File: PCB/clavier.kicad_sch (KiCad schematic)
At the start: 0 parts

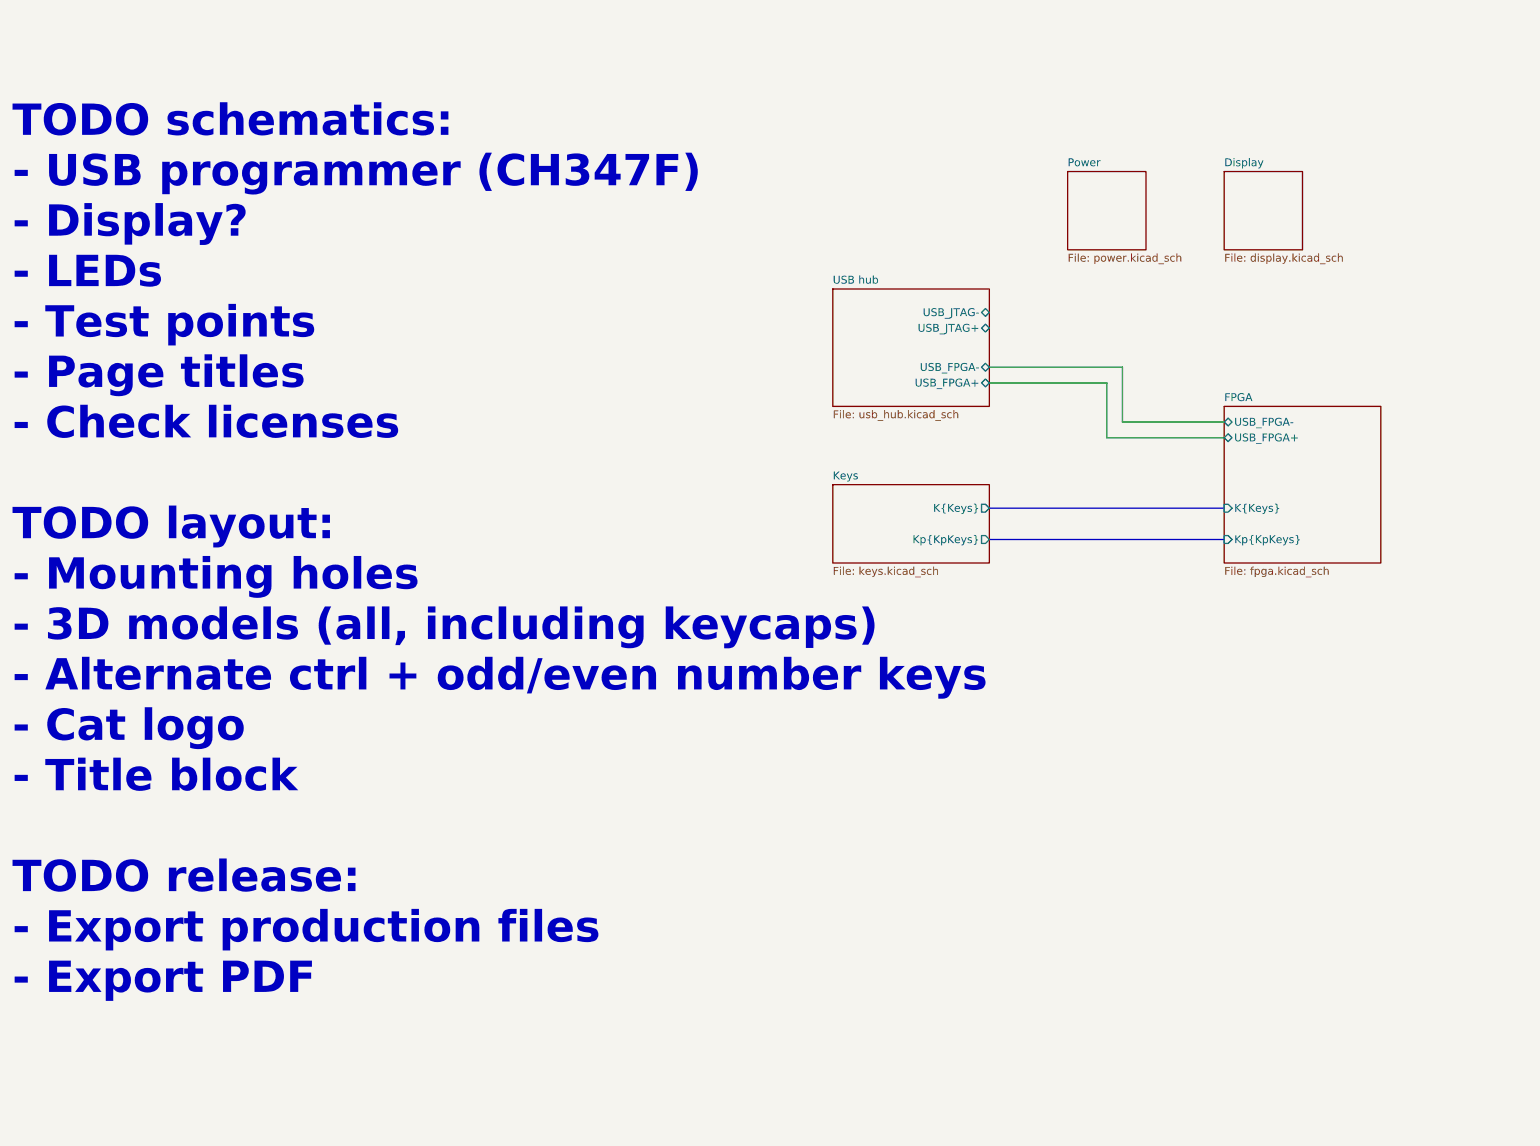
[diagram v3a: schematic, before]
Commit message: Add the USB to JTAG bridge
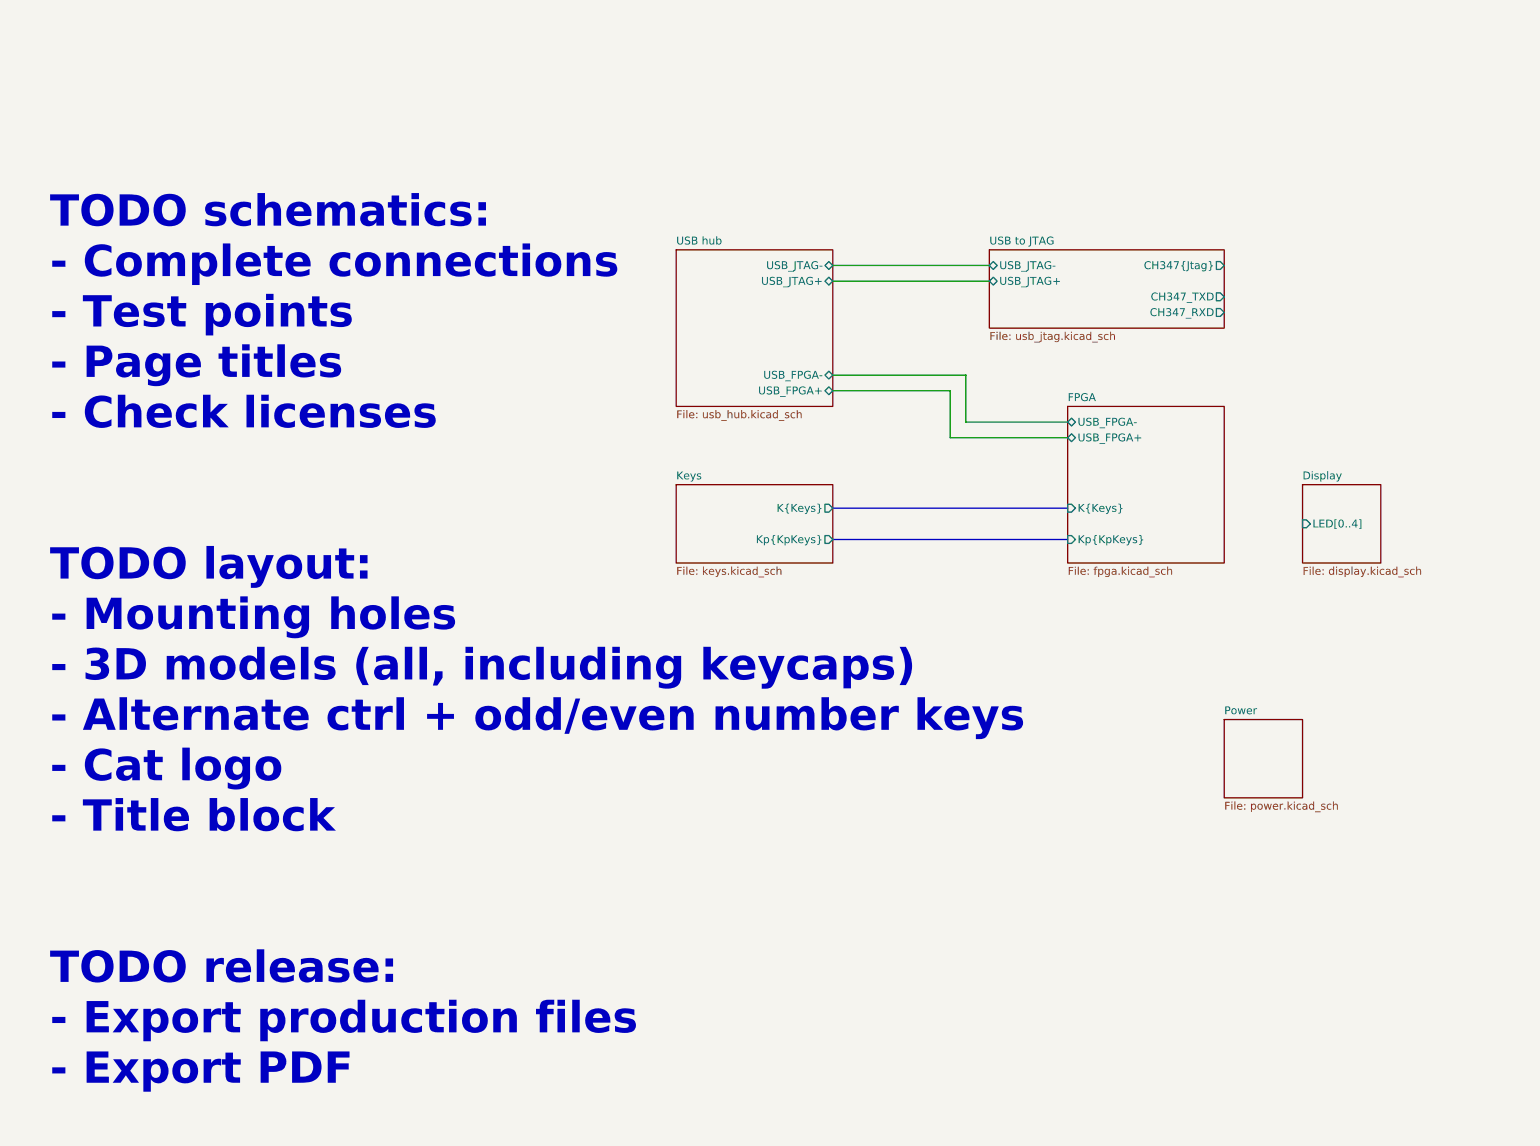
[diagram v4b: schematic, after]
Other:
- added sheet USB to JTAG (usb_jtag.kicad_sch)
- sheet Display ports: added LED[0..4]; removed none
- note added: "TODO schematics: - Complete connections - Test points - Page titles - Check licenses TODO layout: - Mounting holes - 3D models (all, including keycaps) - Alternate ctrl + odd/even number keys - Cat logo - Title block TODO release: - Export production files - Export PDF"
- note removed: "TODO schematics: - USB programmer (CH347F) - Display? - LEDs - Test points - Page titles - Check licenses TODO layout: - Mounting holes - 3D models (all, including keycaps) - Alternate ctrl + odd/even number keys - Cat logo - Title block TODO release: - Export production files - Export PDF"

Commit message: Improve the CH347F schematics and added 3D models
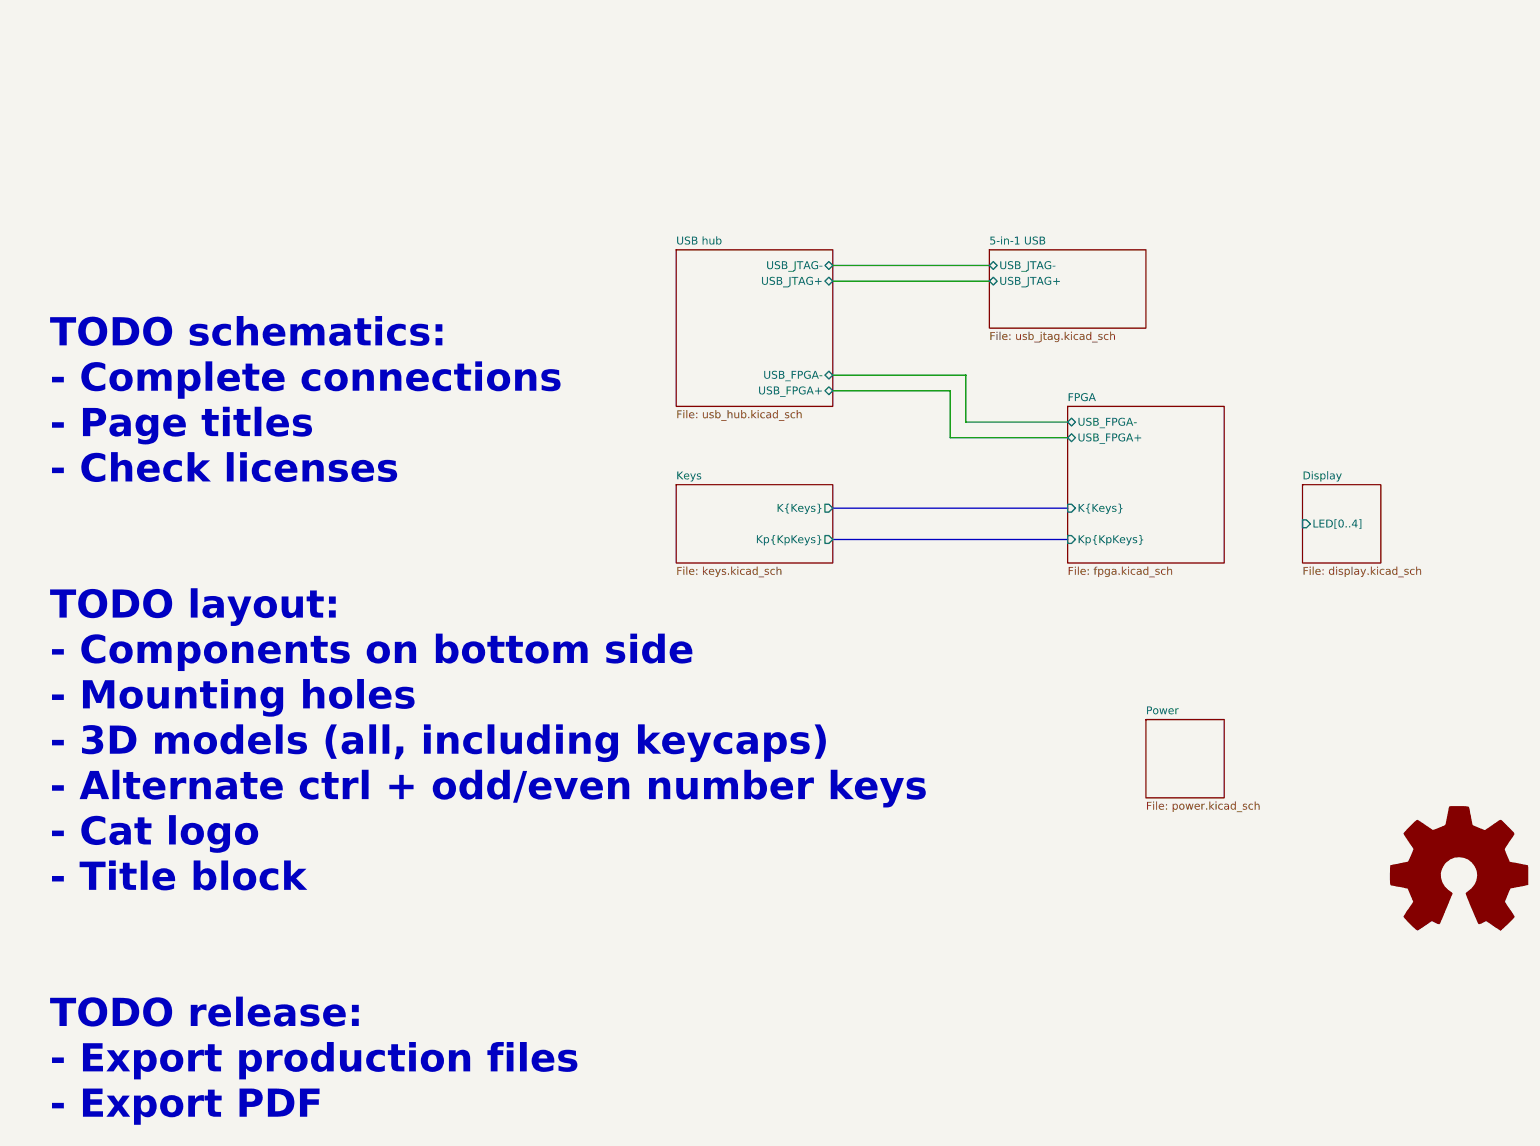
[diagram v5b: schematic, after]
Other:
- sheet USB to JTAG renamed 5-in-1 USB
- sheet 5-in-1 USB ports: added none; removed CH347_RXD, CH347_TXD, CH347{Jtag}
- note added: "TODO schematics: - Complete connections - Page titles - Check licenses TODO layout: - Components on bottom side - Mounting holes - 3D models (all, including keycaps) - Alternate ctrl + odd/even number keys - Cat logo - Title block TODO release: - Export production files - Export PDF"
- note removed: "TODO schematics: - Complete connections - Test points - Page titles - Check licenses TODO layout: - Mounting holes - 3D models (all, including keycaps) - Alternate ctrl + odd/even number keys - Cat logo - Title block TODO release: - Export production files - Export PDF"
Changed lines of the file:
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@@
 	(generator_version "9.0")
 	(paper "A4")
-	(text "TODO schematics:\n- Complete connections\n- Test points\n- Page titles\n- Check licenses\n\n\nTODO layout:\n- Mounting holes\n- 3D models (all, including keycaps)\n- Alternate ctrl + odd/even number keys\n- Cat logo\n- Title block\n\n\nTODO release:\n- Export production files\n- Export PDF"
+	(text "TODO schematics:\n- Complete connections\n- Page titles\n- Check licenses\n\n\nTODO layout:\n- Components on bottom side\n- Mounting holes\n- 3D models (all, including keycaps)\n- Alternate ctrl + odd/even number keys\n- Cat logo\n- Title block\n\n\nTODO release:\n- Export production files\n- Export PDF"
 		(exclude_from_sim no)
-		(at 25.4 114.3 0)
+		(at 25.4 127 0)
 		(effects
 			(font
-				(size 5.08 5.08)
+				(size 4.572 4.572)
 				(thickness 1.016)
 				(bold yes)
@@
 		)
 	)
+	(symbol
+		(lib_id "Graphic:Logo_Open_Hardware_Large")
+		(at 254 152.4 0)
+		(unit 1)
+		(exclude_from_sim yes)
+		(in_bom no)
+		(on_board no)
+		(dnp no)
+		(fields_autoplaced yes)
+		(property "Reference" "#SYM1"
+			(at 254 139.7 0)
+			(effects
+				(font
+					(size 1.27 1.27)
+				)
+				(hide yes)
+			)
+		)
+		(property "Value" "Logo_Open_Hardware_Large"
+			(at 254 162.56 0)
+			(effects
+				(font
+					(size 1.27 1.27)
+				)
+				(hide yes)
+			)
+		)
+		(property "Footprint" ""
+			(at 254 152.4 0)
+			(effects
+				(font
+					(size 1.27 1.27)
+				)
+				(hide yes)
+			)
+		)
+		(property "Datasheet" "~"
+			(at 254 152.4 0)
+			(effects
+				(font
+					(size 1.27 1.27)
+				)
+				(hide yes)
+			)
+		)
+		(property "Description" "Open Hardware logo, large"
+			(at 254 152.4 0)
+			(effects
+				(font
+					(size 1.27 1.27)
+				)
+				(hide yes)
+			)
+		)
+		(instances
+			(project ""
+				(path "/6362c6e0-59ef-40d3-b6e0-7e9dfe7b9b20"
+					(reference "#SYM1")
+					(unit 1)
+				)
+			)
+		)
+	)
 	(sheet
-		(at 215.9 127)
+		(at 203.2 127)
 		(size 12.7 12.7)
 		(exclude_from_sim no)
@@
 		)
 		(property "Sheetname" "Power"
-			(at 215.9 126.2884 0)
+			(at 203.2 126.2884 0)
 			(effects
 				(font
@@
 		)
 		(property "Sheetfile" "power.kicad_sch"
-			(at 215.9 140.2846 0)
+			(at 203.2 140.2846 0)
 			(effects
 				(font
@@
 	(sheet
 		(at 177.8 50.8)
-		(size 38.1 12.7)
+		(size 25.4 12.7)
 		(exclude_from_sim no)
 		(in_bom yes)
@@
 			(color 0 0 0 0.0000)
 		)
-		(property "Sheetname" "USB to JTAG"
+		(property "Sheetname" "5-in-1 USB"
 			(at 177.8 50.0884 0)
 			(effects
@@
 			)
 		)
-		(pin "CH347{Jtag}" output
-			(at 215.9 53.34 0)
-			(effects
-				(font
-					(size 1.27 1.27)
-				)
-				(justify right)
-			)
-		)
-		(pin "CH347_TXD" output
-			(at 215.9 58.42 0)
-			(effects
-				(font
-					(size 1.27 1.27)
-				)
-				(justify right)
-			)
-		)
-		(pin "CH347_RXD" output
-			(at 215.9 60.96 0)
-			(effects
-				(font
-					(size 1.27 1.27)
-				)
-				(justify right)
-			)
-		)

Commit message: Add LICENSE and minor improvements
- Filled the title blocks
- Connected the LEDs to the FPGA
- Changed the FPGA programming header
- Added USB fuse and capacitors
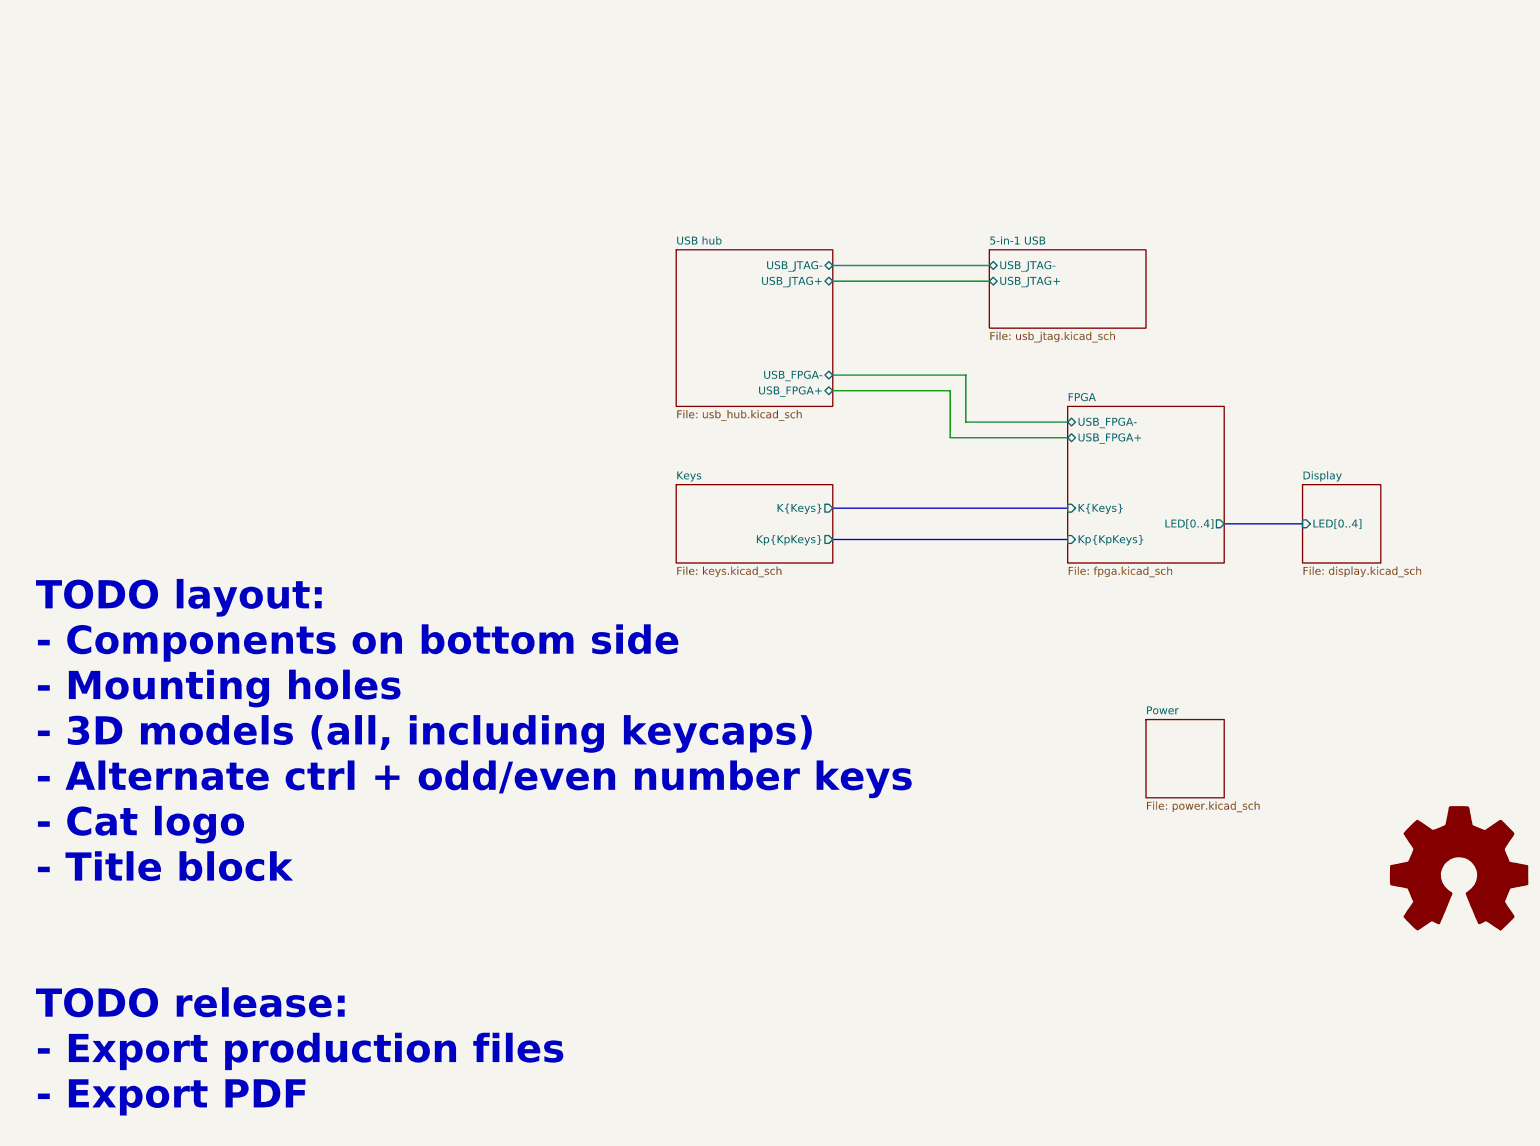
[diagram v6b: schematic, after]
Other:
- sheet FPGA ports: added LED[0..4]; removed none
- note added: "TODO layout: - Components on bottom side - Mounting holes - 3D models (all, including keycaps) - Alternate ctrl + odd/even number keys - Cat logo - Title block TODO release: - Export production files - Export PDF"
- note removed: "TODO schematics: - Complete connections - Page titles - Check licenses TODO layout: - Components on bottom side - Mounting holes - 3D models (all, including keycaps) - Alternate ctrl + odd/even number keys - Cat logo - Title block TODO release: - Export production files - Export PDF"
- company: (none) -> Copyright (c) 2025 L. Sartory
- title: (none) -> Clavier - Overview
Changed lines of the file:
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@@
 	(generator_version "9.0")
 	(paper "A4")
-	(text "TODO schematics:\n- Complete connections\n- Page titles\n- Check licenses\n\n\nTODO layout:\n- Components on bottom side\n- Mounting holes\n- 3D models (all, including keycaps)\n- Alternate ctrl + odd/even number keys\n- Cat logo\n- Title block\n\n\nTODO release:\n- Export production files\n- Export PDF"
+	(title_block
+		(title "Clavier - Overview")
+		(date "2025-06-01")
+		(rev "1.0")
+		(company "Copyright (c) 2025 L. Sartory")
+		(comment 1 "SPDX-License-Identifier: CERN-OHL-P-2.0")
+	)
+	(text "TODO layout:\n- Components on bottom side\n- Mounting holes\n- 3D models (all, including keycaps)\n- Alternate ctrl + odd/even number keys\n- Cat logo\n- Title block\n\n\nTODO release:\n- Export production files\n- Export PDF"
 		(exclude_from_sim no)
-		(at 25.4 127 0)
+		(at 23.114 147.574 0)
 		(effects
 			(font
@@
 		(pts
 			(xy 171.45 73.66) (xy 171.45 81.28)
+		)
+		(stroke
+			(width 0)
+			(type default)
+		)
+	)
+	(bus
+		(pts
+			(xy 215.9 95.25) (xy 228.6 95.25)
 		)
 		(stroke
@@
 			)
 		)
+		(pin "LED[0..4]" output
+			(at 215.9 95.25 0)
+			(effects
+				(font
+					(size 1.27 1.27)
+				)
+				(justify right)
+			)
+		)
